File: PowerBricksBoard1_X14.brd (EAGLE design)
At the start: 76.2 x 53.3 mm, 16 parts

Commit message: Fixed things
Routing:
- net 12_GND: track 73.2 -> 69.2 mm, vias 2 -> 1
- net C2: track 44.5 -> 47.5 mm
- net ALERT: track 35.0 -> 32.0 mm, vias 2 -> 0
- net 48_GND: track 88.8 -> 87.8 mm
- net DATA: track 17.7 -> 17.2 mm
- removed copper zone on layer 1, net 12_GND

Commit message: new
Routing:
- net 12_GND: track 69.2 -> 4.93 mm, vias 1 -> 0
- net 48_GND: vias 1 -> 13
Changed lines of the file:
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@@
 <contactref element="C4" pad="-"/>
 <contactref element="D2" pad="C"/>
-<polygon width="0.1524" layer="1" isolate="0.8128" rank="6">
-<vertex x="-4.572" y="56.896"/>
-<vertex x="-4.572" y="-5.842"/>
-<vertex x="81.28" y="-5.842"/>
-<vertex x="81.28" y="56.896"/>
-</polygon>
-<polygon width="0.1524" layer="16" isolate="0.8128" rank="6">
+<polygon width="1.016" layer="16" isolate="0.8128" rank="6">
 <vertex x="-2.794" y="54.864"/>
 <vertex x="-2.794" y="-3.556"/>
@@
 <wire x1="38.342" y1="49.53" x2="39.612" y2="50.8" width="0.762" layer="1"/>
 <wire x1="39.612" y1="50.8" x2="39.612" y2="50.673" width="0.762" layer="1"/>
+<polygon width="0.254" layer="1">
+<vertex x="43.18" y="9.2075"/>
+<vertex x="50.8" y="9.2075"/>
+<vertex x="50.8" y="3.81"/>
+<vertex x="43.18" y="3.81"/>
+</polygon>
+<via x="44.45" y="7.62" extent="1-16" drill="0.35"/>
+<via x="49.53" y="7.62" extent="1-16" drill="0.35"/>
+<polygon width="0.254" layer="1">
+<vertex x="43.18" y="41.5925"/>
+<vertex x="50.8" y="41.5925"/>
+<vertex x="50.8" y="36.195"/>
+<vertex x="43.18" y="36.195"/>
+</polygon>
+<polygon width="0.254" layer="1">
+<vertex x="43.18" y="25.4"/>
+<vertex x="50.8" y="25.4"/>
+<vertex x="50.8" y="19.3675"/>
+<vertex x="43.18" y="19.3675"/>
+</polygon>
+<via x="44.45" y="21.59" extent="1-16" drill="0.35"/>
+<via x="49.53" y="21.59" extent="1-16" drill="0.35"/>
+<via x="49.53" y="22.86" extent="1-16" drill="0.35"/>
+<via x="44.45" y="22.86" extent="1-16" drill="0.35"/>
+<via x="44.45" y="37.465" extent="1-16" drill="0.35"/>
+<via x="44.45" y="40.005" extent="1-16" drill="0.35"/>
+<via x="49.53" y="40.005" extent="1-16" drill="0.35"/>
+<via x="49.53" y="37.465" extent="1-16" drill="0.35"/>
+<via x="44.45" y="5.08" extent="1-16" drill="0.35"/>
+<via x="49.53" y="5.08" extent="1-16" drill="0.35"/>
 </signal>
 <signal name="12V">
 <contactref element="R1" pad="2"/>
 <contactref element="R5" pad="2"/>
-<polygon width="0.254" layer="1" isolate="0.8128">
+<polygon width="1.016" layer="1" isolate="0.8128">
 <vertex x="2.54" y="50.8"/>
 <vertex x="34.925" y="50.8"/>
@@
 <contactref element="U$1" pad="P02_7"/>
 <contactref element="U$1" pad="P02_8"/>
-<wire x1="12.7" y1="3.175" x2="11.1125" y2="4.7625" width="0.762" layer="16"/>
-<wire x1="12.7" y1="3.175" x2="24.20364375" y2="3.175" width="0.762" layer="16"/>
-<wire x1="24.20364375" y1="3.175" x2="26.84564375" y2="5.817" width="0.762" layer="16"/>
-<wire x1="33.757" y1="5.817" x2="35.56" y2="7.62" width="0.762" layer="16"/>
-<wire x1="26.84564375" y1="5.817" x2="33.757" y2="5.817" width="0.762" layer="16"/>
-<wire x1="35.56" y1="7.62" x2="35.56" y2="21.59" width="0.762" layer="16"/>
-<via x="35.56" y="21.59" extent="1-16" drill="0.35"/>
-<wire x1="35.56" y1="21.59" x2="35.56" y2="30.48" width="0.762" layer="1"/>
-<wire x1="35.56" y1="30.48" x2="33.655" y2="32.385" width="0.762" layer="1"/>
-<wire x1="33.655" y1="32.385" x2="29.53" y2="32.385" width="0.762" layer="1"/>
-<polygon width="0.1524" layer="16" isolate="0.8128">
-<vertex x="-1.27" y="55.88"/>
-<vertex x="-1.27" y="11.43"/>
-<vertex x="36.195" y="11.43"/>
-<vertex x="36.195" y="55.88"/>
-</polygon>
 <contactref element="U$2" pad="5"/>
 <contactref element="U$1" pad="P02_5"/>
+<polygon width="1.016" layer="16">
+<vertex x="0" y="54.61"/>
+<vertex x="17.78" y="54.61"/>
+<vertex x="31.75" y="54.61"/>
+<vertex x="33.02" y="53.34"/>
+<vertex x="34.29" y="52.07"/>
+<vertex x="34.29" y="30.48"/>
+<vertex x="33.02" y="29.21"/>
+<vertex x="20.32" y="29.21"/>
+<vertex x="19.05" y="29.21"/>
+<vertex x="13.97" y="34.29"/>
+<vertex x="8.89" y="34.29"/>
+<vertex x="7.62" y="33.02"/>
+<vertex x="7.62" y="17.78"/>
+<vertex x="8.89" y="16.51"/>
+<vertex x="10.16" y="17.78"/>
+<vertex x="10.16" y="20.32"/>
+<vertex x="10.16" y="21.59"/>
+<vertex x="11.43" y="22.86"/>
+<vertex x="12.7" y="22.86"/>
+<vertex x="17.78" y="22.86"/>
+<vertex x="19.05" y="21.59"/>
+<vertex x="20.32" y="20.32"/>
+<vertex x="20.32" y="7.62"/>
+<vertex x="11.43" y="-1.27"/>
+<vertex x="-1.27" y="-1.27"/>
+<vertex x="-6.35" y="3.81"/>
+<vertex x="-6.35" y="21.59"/>
+<vertex x="-6.35" y="48.26"/>
+</polygon>
 <wire x1="17.145" y1="32.778" x2="21.517" y2="32.778" width="0.762" layer="1"/>
 <wire x1="21.517" y1="32.778" x2="21.91" y2="32.385" width="0.762" layer="1"/>
-<polygon width="0.1524" layer="16">
-<vertex x="10.16" y="21.59"/>
-<vertex x="15.24" y="21.59"/>
-<vertex x="16.51" y="20.32"/>
-<vertex x="16.51" y="8.255"/>
-<vertex x="3.175" y="8.255"/>
-<vertex x="3.175" y="10.795"/>
-<vertex x="10.16" y="17.78"/>
-</polygon>
-<wire x1="11.1125" y1="4.7625" x2="11.1125" y2="12.3825" width="0.762" layer="16"/>
 </signal>
 <signal name="ALERT">
@@
 <contactref element="C2" pad="+"/>
 <contactref element="C4" pad="+"/>
-<polygon width="0.254" layer="1" isolate="0.8128">
+<polygon width="1.016" layer="1" isolate="0.8128">
 <vertex x="39.37" y="20.955"/>
 <vertex x="20.32" y="20.955"/>
 <vertex x="20.32" y="13.97"/>
 <vertex x="39.37" y="13.97"/>
-</polygon>
-<polygon width="0.254" layer="1" isolate="0.8128">
-<vertex x="39.37" y="49.53"/>
-<vertex x="44.45" y="49.53"/>
-<vertex x="44.45" y="2.54"/>
-<vertex x="39.37" y="2.54"/>
 </polygon>
 <contactref element="U$2" pad="1"/>
@@
 <contactref element="U$1" pad="P03_7"/>
 <contactref element="U$1" pad="P03_8"/>
-<polygon width="0.762" layer="1" isolate="0.6096">
-<vertex x="43.18" y="48.895"/>
-<vertex x="53.34" y="48.895"/>
-<vertex x="53.34" y="43.18"/>
-<vertex x="43.18" y="43.18"/>
-</polygon>
-<polygon width="0.762" layer="1" isolate="0.8128">
-<vertex x="43.18" y="34.29"/>
-<vertex x="64.77" y="34.29"/>
-<vertex x="64.77" y="26.67"/>
-<vertex x="43.18" y="26.67"/>
-</polygon>
-<polygon width="0.762" layer="1" isolate="0.8128">
-<vertex x="53.34" y="18.415"/>
-<vertex x="53.34" y="10.795"/>
-<vertex x="43.815" y="10.795"/>
-<vertex x="43.815" y="18.415"/>
-</polygon>
-</signal>
+<polygon width="1.016" layer="1" rank="4">
+<vertex x="40.64" y="60.96"/>
+<vertex x="33.02" y="53.34"/>
+<vertex x="33.02" y="-6.35"/>
+<vertex x="35.56" y="-8.89"/>
+<vertex x="55.88" y="-8.89"/>
+<vertex x="69.85" y="-8.89"/>
+<vertex x="85.09" y="6.35"/>
+<vertex x="85.09" y="54.61"/>
+<vertex x="78.74" y="60.96"/>
+</polygon>
+</signal>

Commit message: final
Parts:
- moved D1 17.6 mm to (1.91, 24.8)
- moved R1 17.6 mm to (1.91, 28.6)
- moved U$2 8.89 mm to (71.1, 31.8)
- moved C1 8.89 mm to (55.9, 43.2)
- moved C2 8.89 mm to (55.9, 26.7)
- moved C4 8.89 mm to (55.9, 10.8)
- moved R2 8.89 mm to (47.0, 45.7)
- moved R3 8.89 mm to (12.7, 25.4)
- moved R4 8.89 mm to (12.7, 30.5)
- moved R5 8.89 mm to (25.4, 24.1)
- moved U$1 8.89 mm to (36.8, 25.4)
- moved D2 8.89 mm to (46.4, 49.5)
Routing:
- net 48_GND: track 87.8 -> 26.5 mm, vias 13 -> 17
- net 12_GND: track 4.93 -> 1.03 mm, vias 0 -> 1
- net ON/OFF: vias 2 -> 1

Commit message: more adjustments
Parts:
- removed U$1: CONN_BRICKS, CONN, Distribution-Bricks:SAMTEC_PESC-02-12-02-01-X-VT-LC
- added J1: PESC-02-12-02-01-X-VT-LC(BRICKS-DISTRIBUTION), CONN, Distribution-Bricks:SAMTEC_PESC-02-12-02-01-X-VT-LC(B-D)
- moved D2 51.5 mm to (60.6, 0.00)
- moved R2 46.6 mm to (55.9, 0.00), turned to 180 degrees
- moved C1 1.02 mm to (55.9, 42.2)
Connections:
- net 12V: now also J1.P01_1, J1.P01_2, J1.P01_3, J1.P01_4, J1.P01_5, J1.P01_6, J1.P01_7, J1.P01_8; no longer U$1.P01_1, U$1.P01_2, U$1.P01_3, U$1.P01_4, U$1.P01_5, U$1.P01_6, U$1.P01_7, U$1.P01_8
- net 12_GND: now also J1.P02_1, J1.P02_2, J1.P02_3, J1.P02_4, J1.P02_5, J1.P02_6, J1.P02_7, J1.P02_8; no longer U$1.P02_1, U$1.P02_2, U$1.P02_3, U$1.P02_4, U$1.P02_5, U$1.P02_6, U$1.P02_7, U$1.P02_8
- net 48V: now also J1.P03_1, J1.P03_2, J1.P03_3, J1.P03_4, J1.P03_5, J1.P03_6, J1.P03_7, J1.P03_8; no longer U$1.P03_1, U$1.P03_2, U$1.P03_3, U$1.P03_4, U$1.P03_5, U$1.P03_6, U$1.P03_7, U$1.P03_8
- net 48_GND: now also J1.P04_1, J1.P04_2, J1.P04_3, J1.P04_4, J1.P04_5, J1.P04_6, J1.P04_7, J1.P04_8; no longer U$1.P04_1, U$1.P04_2, U$1.P04_3, U$1.P04_4, U$1.P04_5, U$1.P04_6, U$1.P04_7, U$1.P04_8
- net ALERT: now also J1.02; no longer U$1.01
- net C2: now also J1.04; no longer U$1.02
- net CLK: now also J1.03; no longer U$1.03
- net DATA: now also J1.01; no longer U$1.04
- net ON/OFF: now also J1.05; no longer U$1.05
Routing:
- net ON/OFF: track 33.2 -> 79.7 mm, vias 1 -> 0
- net C2: track 47.5 -> 19.2 mm
- net 48_GND: track 26.5 -> 1.54 mm, vias 17 -> 13
- net ALERT: track 32.0 -> 21.4 mm
- net DATA: track 17.2 -> 24.1 mm, vias 2 -> 0
- net N$2: track 4.08 -> 2.97 mm
- added copper zone on layer 1, net 12_GND

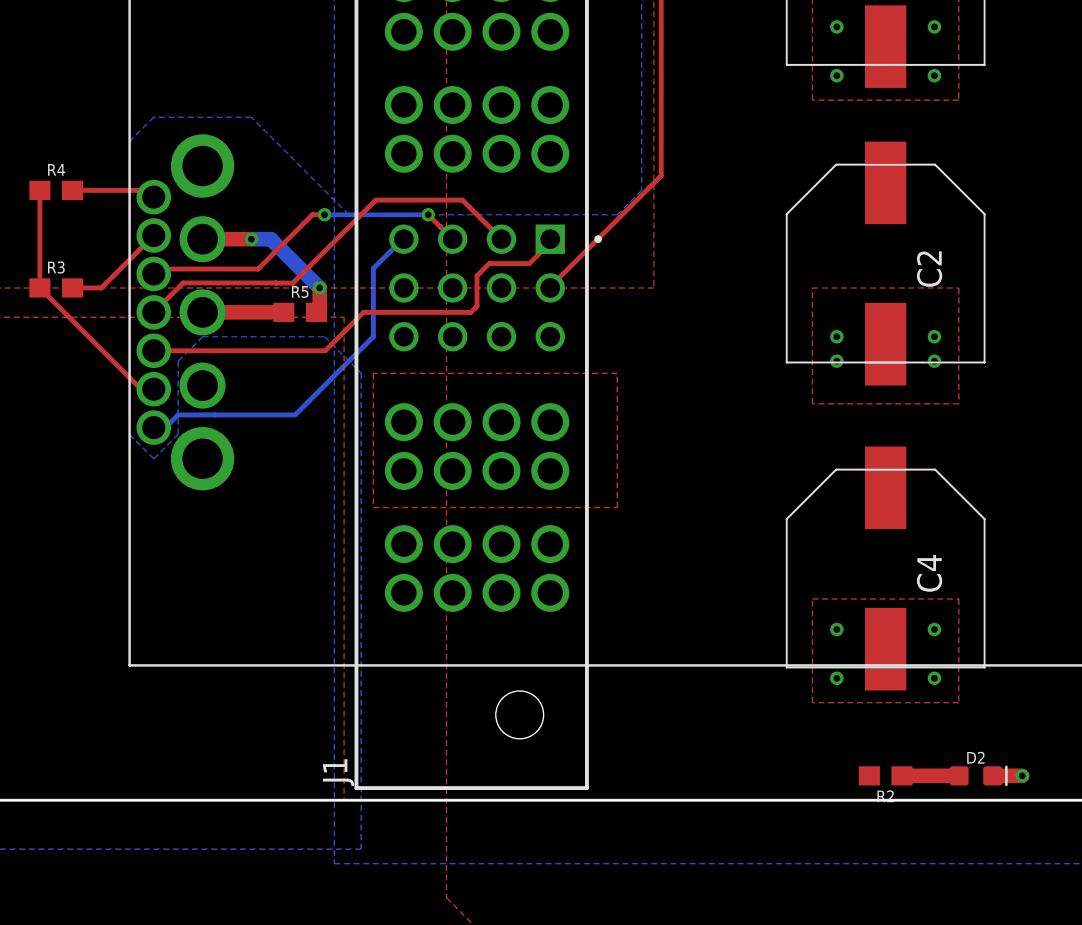
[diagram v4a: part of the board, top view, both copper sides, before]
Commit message: Final Touches
I implemented the final design suggestions, sorry it was so late
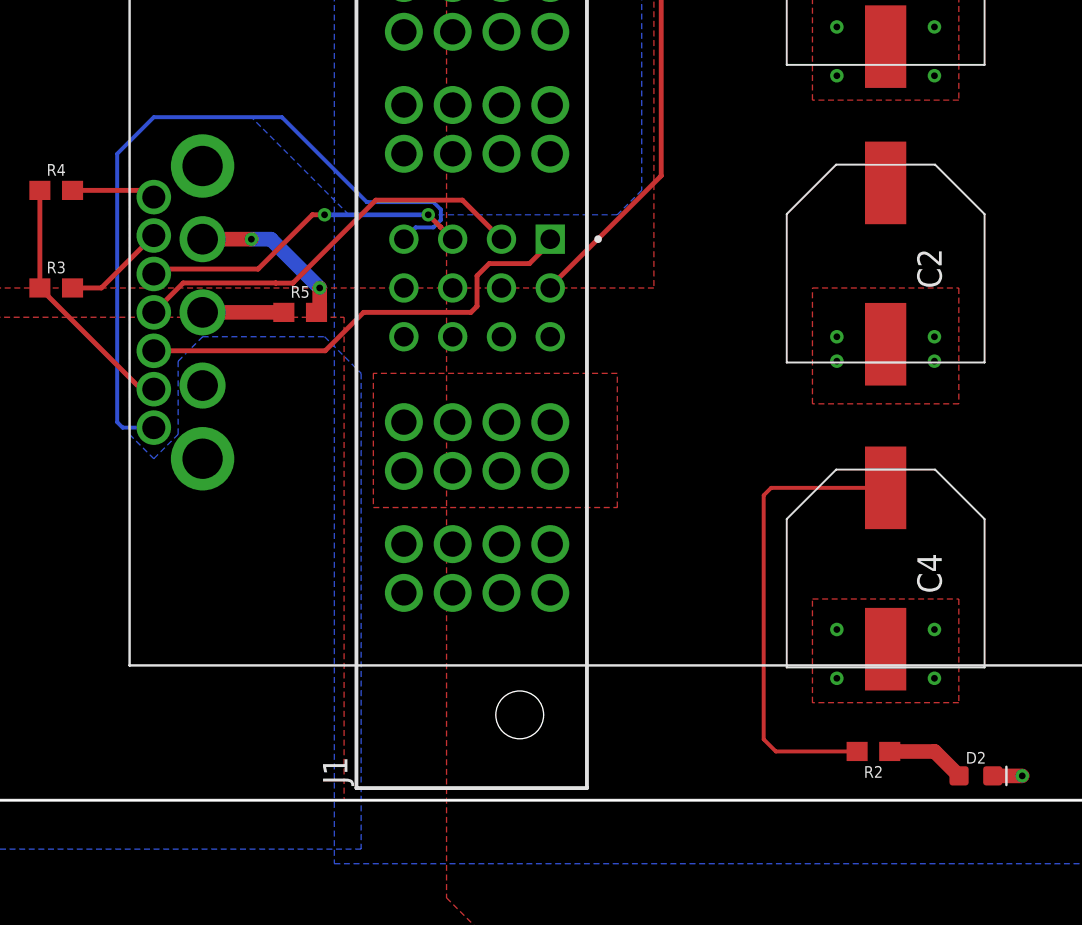
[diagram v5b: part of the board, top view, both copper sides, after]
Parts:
- moved R2 1.42 mm to (55.2, 1.27)
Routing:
- net 48V: track 0.00 -> 24.3 mm
- net C2: track 19.2 -> 38.5 mm
- net N$2: track 2.97 -> 4.13 mm
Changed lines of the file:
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@@
 <?xml version="1.0" encoding="utf-8"?>
 <!DOCTYPE eagle SYSTEM "eagle.dtd">
-<eagle version="9.5.0">
+<eagle version="9.6.2">
 <drawing>
 <settings>
@@
 <attribute name="VALUE" x="2.667" y="28.575" size="0.6096" layer="27" font="vector" ratio="20" rot="R90" align="top-center"/>
 </element>
-<element name="R2" library="SparkFun-Resistors" library_urn="urn:adsk.eagle:library:532" package="0603" package3d_urn="urn:adsk.eagle:package:39650/1" value="2400" x="55.88" y="0" smashed="yes" rot="R180">
-<attribute name="NAME" x="55.88" y="-0.762" size="0.6096" layer="25" font="vector" ratio="20" rot="R180" align="bottom-center"/>
-<attribute name="PROD_ID" value=" " x="22.86" y="68.58" size="1.778" layer="27" rot="R180" display="off"/>
-<attribute name="VALUE" x="55.88" y="0.762" size="0.6096" layer="27" font="vector" ratio="20" rot="R180" align="top-center"/>
+<element name="R2" library="SparkFun-Resistors" library_urn="urn:adsk.eagle:library:532" package="0603" package3d_urn="urn:adsk.eagle:package:39650/1" value="2400" x="55.245" y="1.27" smashed="yes" rot="R180">
+<attribute name="NAME" x="55.245" y="0.508" size="0.6096" layer="25" font="vector" ratio="20" rot="R180" align="bottom-center"/>
+<attribute name="PROD_ID" value=" " x="22.225" y="69.85" size="1.778" layer="27" rot="R180" display="off"/>
+<attribute name="VALUE" x="55.245" y="2.032" size="0.6096" layer="27" font="vector" ratio="20" rot="R180" align="top-center"/>
 </element>
 <element name="R3" library="SparkFun-Resistors" library_urn="urn:adsk.eagle:library:532" package="0603" package3d_urn="urn:adsk.eagle:package:39650/1" value=" " x="12.7" y="25.4" smashed="yes">
@@
 <contactref element="U$2" pad="10"/>
 <contactref element="J1" pad="04"/>
-<wire x1="17.78" y1="18.13" x2="18.384" y2="18.13" width="0.254" layer="16"/>
-<wire x1="20.95383125" y1="18.7898" x2="20.96003125" y2="18.796" width="0.254" layer="16"/>
-<wire x1="19.0438" y1="18.7898" x2="20.95383125" y2="18.7898" width="0.254" layer="16"/>
-<wire x1="25.146" y1="18.796" x2="29.21" y2="22.86" width="0.254" layer="16"/>
-<wire x1="29.21" y1="22.86" x2="29.21" y2="26.416" width="0.254" layer="16"/>
-<wire x1="29.21" y1="26.416" x2="30.734" y2="27.94" width="0.254" layer="16"/>
-<wire x1="30.734" y1="27.94" x2="30.8" y2="27.94" width="0.254" layer="16"/>
-<wire x1="18.384" y1="18.13" x2="19.0438" y2="18.7898" width="0.254" layer="16"/>
-<wire x1="20.96003125" y1="18.796" x2="25.146" y2="18.796" width="0.254" layer="16"/>
+<wire x1="17.78" y1="18.13" x2="16.16" y2="18.13" width="0.2032" layer="16"/>
+<wire x1="16.16" y1="18.13" x2="15.875" y2="18.415" width="0.2032" layer="16"/>
+<wire x1="15.875" y1="18.415" x2="15.875" y2="32.385" width="0.2032" layer="16"/>
+<wire x1="15.875" y1="32.385" x2="17.78" y2="34.29" width="0.2032" layer="16"/>
+<wire x1="32.3398875" y1="29.8676" x2="32.7251" y2="29.4823875" width="0.2032" layer="16"/>
+<wire x1="32.7251" y1="29.4823875" x2="32.7251" y2="28.9376125" width="0.2032" layer="16"/>
+<wire x1="32.7251" y1="28.9376125" x2="32.3398875" y2="28.5524" width="0.2032" layer="16"/>
+<wire x1="24.45" y1="34.29" x2="28.8724" y2="29.8676" width="0.2032" layer="16"/>
+<wire x1="32.3398875" y1="28.5524" x2="31.4124" y2="28.5524" width="0.2032" layer="16"/>
+<wire x1="31.4124" y1="28.5524" x2="30.8" y2="27.94" width="0.2032" layer="16"/>
+<wire x1="28.8724" y1="29.8676" x2="32.3398875" y2="29.8676" width="0.2032" layer="16"/>
+<wire x1="17.78" y1="34.29" x2="24.45" y2="34.29" width="0.2032" layer="16"/>
 </signal>
 <signal name="12_GND">
@@
 <contactref element="D2" pad="A"/>
 <contactref element="R2" pad="1"/>
-<wire x1="56.73" y1="0" x2="59.702" y2="0" width="0.762" layer="1"/>
+<wire x1="58.432" y1="1.27" x2="56.095" y2="1.27" width="0.762" layer="1"/>
+<wire x1="58.432" y1="1.27" x2="59.702" y2="0" width="0.762" layer="1"/>
 </signal>
 <signal name="DGND">
@@
 </polygon>
 <contactref element="U$2" pad="1"/>
-<polygon width="1.016" layer="1" rank="4">
+<polygon width="1.016" layer="1" isolate="1.27" rank="4">
 <vertex x="40.64" y="60.96"/>
 <vertex x="33.02" y="53.34"/>
@@
 <contactref element="J1" pad="P03_3"/>
 <contactref element="J1" pad="P03_4"/>
+<wire x1="54.395" y1="1.27" x2="50.165" y2="1.27" width="0.2032" layer="1"/>
+<wire x1="50.165" y1="1.27" x2="49.53" y2="1.905" width="0.2032" layer="1"/>
+<wire x1="49.53" y1="1.905" x2="49.53" y2="14.605" width="0.2032" layer="1"/>
+<wire x1="49.53" y1="14.605" x2="49.92" y2="14.995" width="0.2032" layer="1"/>
+<wire x1="49.92" y1="14.995" x2="55.88" y2="14.995" width="0.2032" layer="1"/>
 </signal>
 </signals>
